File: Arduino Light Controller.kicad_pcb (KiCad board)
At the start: 2 copper layers, 120.5 x 39 mm, 44 parts, among them J1 Terminal - Pin - Male - 1x2 -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, J10 Terminal - Pin - Male - 1x2 -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, J11 Terminal - Pin - Male - 1x2 -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, J12 Terminal - Pin - Male - 1x2 -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, J13 Terminal - Pin - Male - 1x2 -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, J14 Terminal - Pin - Male - 1x2 -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, J15 Terminal - Pin - Male - 1x2 -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, J16 Terminal - Pin - Male - 1x2 -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, J17 Terminal - Pin - Male - 1x2 -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, J18 Terminal - Pin - Male - 1x2 -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, J19 Terminal - Pin - Male - 1x4 -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, J2 Terminal - Pin - Male - 1x2 -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, J20 Terminal - Pin - Male - 1x4 -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, J21 Terminal - Pin - Male - 1x4 -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, J22 Terminal - Pin - Male - 1x4 -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, J3 Terminal - Pin - Male - 1x2 -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, J4 Terminal - Pin - Male - 1x2 -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, J5 Terminal - Pin - Male - 1x2 -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, J6 Terminal - Pin - Male - 1x2 -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, J7 Terminal - Pin - Male - 1x2 -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, J8 Terminal - Pin - Male - 1x2 -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, J9 Terminal - Pin - Male - 1x2 -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

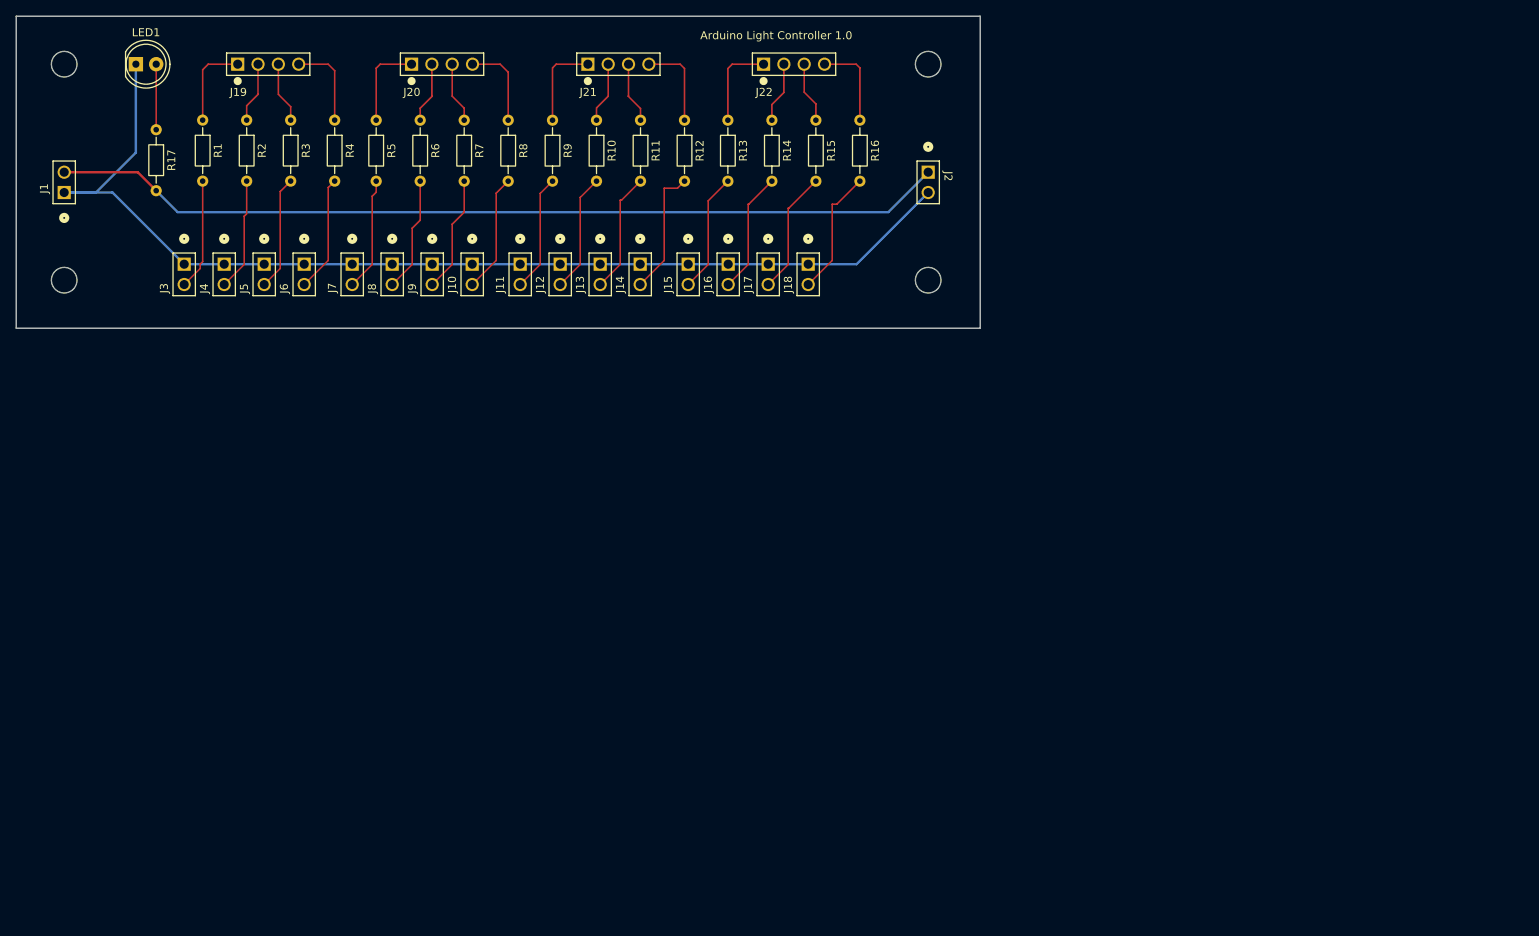
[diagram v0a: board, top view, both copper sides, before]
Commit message: New design to align with other boards and support power bus.
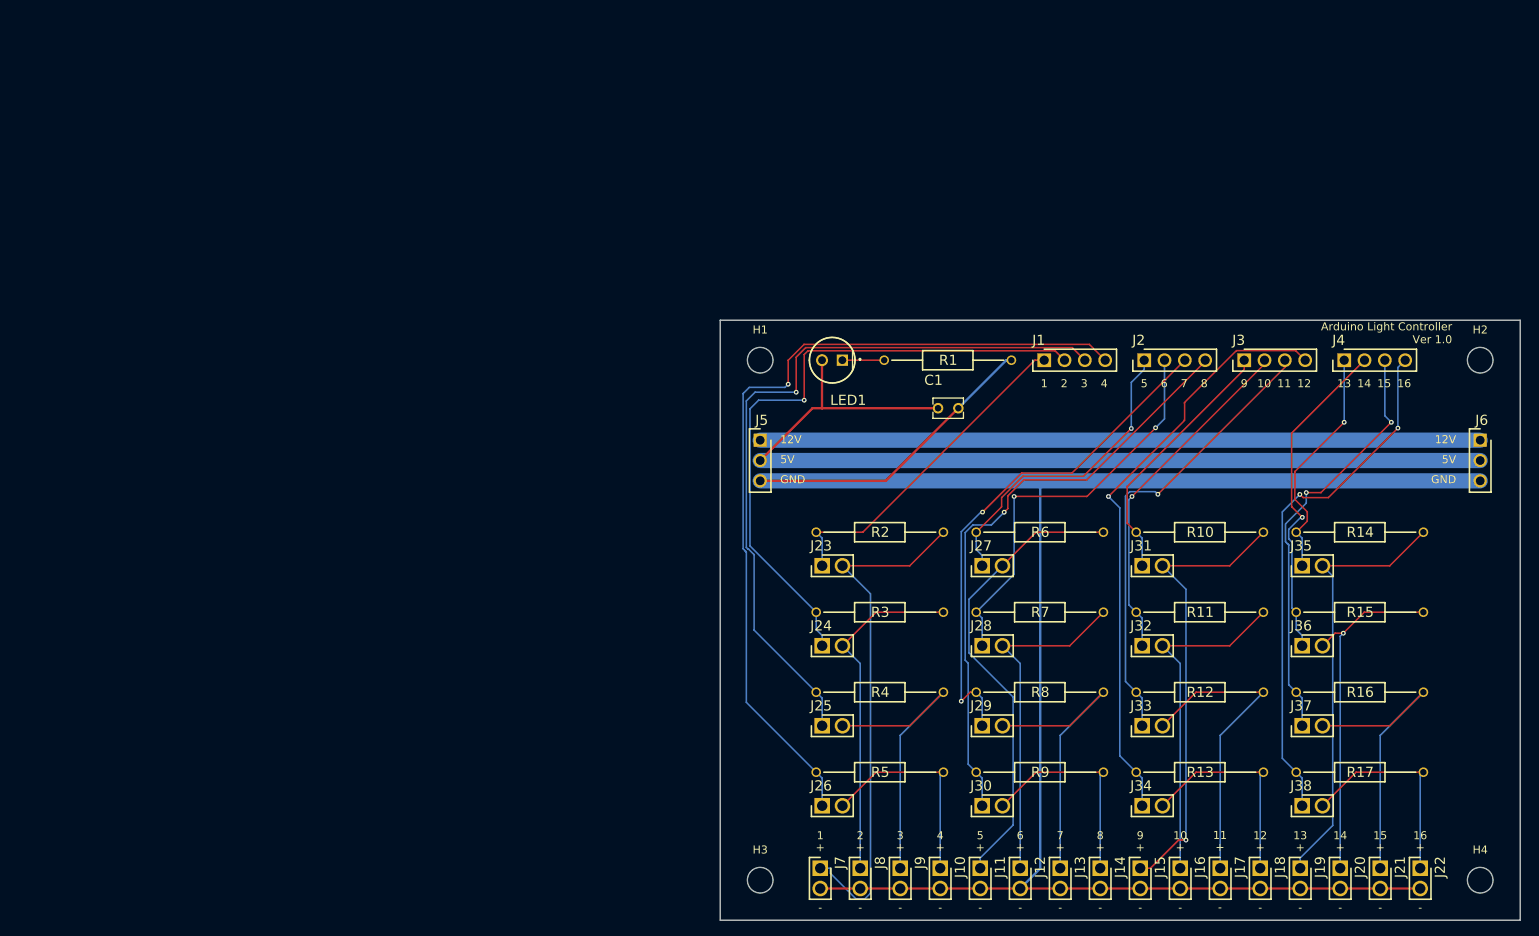
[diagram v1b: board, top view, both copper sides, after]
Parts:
- added C1: C315C104M5U5TA, SamacSys_Parts:C315C100J2G5TA, F.Cu at (128.5, 61.0)
- added J23: 61300211121, SamacSys_Parts:HDRV2W110P0X254_1X2_508X254X854P, F.Cu at (112.7, 80.7)
- added J24: 61300211121, SamacSys_Parts:HDRV2W110P0X254_1X2_508X254X854P, F.Cu at (112.7, 90.7)
- added J25: 61300211121, SamacSys_Parts:HDRV2W110P0X254_1X2_508X254X854P, F.Cu at (112.7, 100.7)
- added J26: 61300211121, SamacSys_Parts:HDRV2W110P0X254_1X2_508X254X854P, F.Cu at (112.7, 110.7)
- added J27: 61300211121, SamacSys_Parts:HDRV2W110P0X254_1X2_508X254X854P, F.Cu at (132.7, 80.7)
- added J28: 61300211121, SamacSys_Parts:HDRV2W110P0X254_1X2_508X254X854P, F.Cu at (132.7, 90.7)
- added J29: 61300211121, SamacSys_Parts:HDRV2W110P0X254_1X2_508X254X854P, F.Cu at (132.7, 100.7)
- added J30: 61300211121, SamacSys_Parts:HDRV2W110P0X254_1X2_508X254X854P, F.Cu at (132.7, 110.7)
- added J31: 61300211121, SamacSys_Parts:HDRV2W110P0X254_1X2_508X254X854P, F.Cu at (152.7, 80.7)
- added J32: 61300211121, SamacSys_Parts:HDRV2W110P0X254_1X2_508X254X854P, F.Cu at (152.7, 90.7)
- added J33: 61300211121, SamacSys_Parts:HDRV2W110P0X254_1X2_508X254X854P, F.Cu at (152.7, 100.7)
- added J34: 61300211121, SamacSys_Parts:HDRV2W110P0X254_1X2_508X254X854P, F.Cu at (152.7, 110.7)
- added J35: 61300211121, SamacSys_Parts:HDRV2W110P0X254_1X2_508X254X854P, F.Cu at (172.7, 80.7)
- added J36: 61300211121, SamacSys_Parts:HDRV2W110P0X254_1X2_508X254X854P, F.Cu at (172.7, 90.7)
- added J37: 61300211121, SamacSys_Parts:HDRV2W110P0X254_1X2_508X254X854P, F.Cu at (172.7, 100.7)
- added J38: 61300211121, SamacSys_Parts:HDRV2W110P0X254_1X2_508X254X854P, F.Cu at (172.7, 110.7)
- J1, J2, J3, J4: value Terminal - Pin - Male - 1x2 - 61300211121 -> 61300411121; footprint Digikey:Terminal - Pin - Male - 1x2 - 61300211121 -> SamacSys_Parts:HDRV4W95P0X254_1X4_1016X254X854P
- J10, J11, J12, J13, J14, J15, J16, J17, J18, J7, J8, J9: value Terminal - Pin - Male - 1x2 - 61300211121 -> 61300211121; footprint Digikey:Terminal - Pin - Male - 1x2 - 61300211121 -> SamacSys_Parts:HDRV2W110P0X254_1X2_508X254X854P
- J19, J20, J21, J22: value Terminal - Pin - Male - 1x4 - 61300411121 -> 61300211121; footprint Digikey:Terminal - Pin - Male - 1x4 - 61300411121 -> SamacSys_Parts:HDRV2W110P0X254_1X2_508X254X854P
- J5, J6: value Terminal - Pin - Male - 1x2 - 61300211121 -> 61300311121; footprint Digikey:Terminal - Pin - Male - 1x2 - 61300211121 -> SamacSys_Parts:HDRV3W64P0X254_1X3_762X254X869P
- LED1: value LED - Green - 5mm - LTL-307G -> WP7113GD; footprint Digikey:LED - Green - 5mm - LTL-307G -> SamacSys_Parts:L53ND
- R1, R10, R11, R12, R13, R14, R15, R16, R17, R2, R3, R4, R5, R6, R7, R8, R9: value 1K -> CFR-25JB-52-1K; footprint Resistor_THT:R_Axial_DIN0204_L3.6mm_D1.6mm_P7.62mm_Horizontal -> SamacSys_Parts:RESAD1590W60L630D240
- moved H4 192.2 mm to (195.0, 120.0)
- moved J19 166.5 mm to (172.5, 118.5), turned to -90 degrees
- moved R17 163.6 mm to (172.0, 106.5), turned to 0 degrees
- moved J20 153.5 mm to (177.5, 118.5), turned to -90 degrees
- moved J6 148.6 mm to (195.0, 65.0)
- moved J21 141.1 mm to (182.5, 118.5), turned to -90 degrees
- moved J4 140.5 mm to (178.0, 55.0), turned to 0 degrees
- moved J3 133.0 mm to (165.5, 55.0), turned to 0 degrees
- moved J22 129.8 mm to (187.5, 118.5), turned to -90 degrees
- moved J1 124.3 mm to (140.5, 55.0), turned to 0 degrees
- moved R5 98.3 mm to (112.0, 106.5), turned to 0 degrees
- moved R9 97.2 mm to (132.0, 106.5), turned to 0 degrees
- moved R13 96.2 mm to (152.0, 106.5), turned to 0 degrees
- moved LED1 95.7 mm to (115.3, 55.0), turned to 180 degrees
- moved J10 95.5 mm to (127.5, 118.5)
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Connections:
- J1 pad 1: GND -> /ResistorNet/In
- J1 pad 2: +5V -> /ResistorNet1/In
- J10 pad 1: GND -> /ResistorNet3/Out
- J10 pad 2: Net-(J10-Pad2) -> GND
- J11 pad 1: GND -> /ResistorNet4/Out
- J11 pad 2: Net-(J11-Pad2) -> GND
- J12 pad 1: GND -> /ResistorNet5/Out
- J12 pad 2: Net-(J12-Pad2) -> GND
- J13 pad 1: GND -> /ResistorNet6/Out
- J13 pad 2: Net-(J13-Pad2) -> GND
- J14 pad 1: GND -> /ResistorNet7/Out
- J14 pad 2: Net-(J14-Pad2) -> GND
- J15 pad 1: GND -> /ResistorNet8/Out
- J15 pad 2: Net-(J15-Pad2) -> GND
- J16 pad 1: GND -> /ResistorNet9/Out
- J16 pad 2: Net-(J16-Pad2) -> GND
- J17 pad 1: GND -> /ResistorNet10/Out
- J17 pad 2: Net-(J17-Pad2) -> GND
- J18 pad 1: GND -> /ResistorNet11/Out
- J18 pad 2: Net-(J18-Pad2) -> GND
- J19 pad 1: Net-(J19-Pad1) -> /ResistorNet12/Out
- J19 pad 2: Net-(J19-Pad2) -> GND
- J2 pad 1: +5V -> /ResistorNet4/In
- J2 pad 2: GND -> /ResistorNet5/In
- J20 pad 1: Net-(J20-Pad1) -> /ResistorNet13/Out
- J20 pad 2: Net-(J20-Pad2) -> GND
- J21 pad 1: Net-(J21-Pad1) -> /ResistorNet14/Out
- J21 pad 2: Net-(J21-Pad2) -> GND
- J22 pad 1: Net-(J22-Pad1) -> /ResistorNet15/Out
- J22 pad 2: Net-(J22-Pad2) -> GND
- J3 pad 1: GND -> /ResistorNet8/In
- J3 pad 2: Net-(J3-Pad2) -> /ResistorNet9/In
- J4 pad 1: GND -> /ResistorNet12/In
- J4 pad 2: Net-(J4-Pad2) -> /ResistorNet13/In
- J5 pad 1: GND -> +12V
- J5 pad 2: Net-(J5-Pad2) -> +5V
- J6 pad 1: GND -> +12V
- J6 pad 2: Net-(J6-Pad2) -> +5V
- J7 pad 1: GND -> /ResistorNet/Out
- J7 pad 2: Net-(J7-Pad2) -> GND
- J8 pad 1: GND -> /ResistorNet1/Out
- J8 pad 2: Net-(J8-Pad2) -> GND
- J9 pad 1: GND -> /ResistorNet2/Out
- J9 pad 2: Net-(J9-Pad2) -> GND
- LED1 pad 1: GND -> Net-(LED1-K)
- LED1 pad 2: Net-(LED1-A) -> +5V
- R1 pad 1: Net-(J19-Pad1) -> Net-(LED1-K)
- R1 pad 2: Net-(J3-Pad2) -> GND
- R10 pad 1: Net-(J21-Pad2) -> /ResistorNet8/In
- R10 pad 2: Net-(J12-Pad2) -> /ResistorNet8/Out
- R11 pad 1: Net-(J21-Pad3) -> /ResistorNet9/In
- R11 pad 2: Net-(J13-Pad2) -> /ResistorNet9/Out
- R12 pad 1: Net-(J21-Pad4) -> /ResistorNet10/In
- R12 pad 2: Net-(J14-Pad2) -> /ResistorNet10/Out
- R13 pad 1: Net-(J22-Pad1) -> /ResistorNet11/In
- R13 pad 2: Net-(J15-Pad2) -> /ResistorNet11/Out
- R14 pad 1: Net-(J22-Pad2) -> /ResistorNet12/In
- R14 pad 2: Net-(J16-Pad2) -> /ResistorNet12/Out
- R15 pad 1: Net-(J22-Pad3) -> /ResistorNet13/In
- R15 pad 2: Net-(J17-Pad2) -> /ResistorNet13/Out
- R16 pad 1: Net-(J22-Pad4) -> /ResistorNet14/In
- R16 pad 2: Net-(J18-Pad2) -> /ResistorNet14/Out
- R17 pad 1: Net-(LED1-A) -> /ResistorNet15/In
- R17 pad 2: +5V -> /ResistorNet15/Out
- R2 pad 1: Net-(J19-Pad2) -> /ResistorNet/In
- R2 pad 2: Net-(J4-Pad2) -> /ResistorNet/Out
- R3 pad 1: Net-(J19-Pad3) -> /ResistorNet1/In
- R3 pad 2: Net-(J5-Pad2) -> /ResistorNet1/Out
- R4 pad 1: Net-(J19-Pad4) -> /ResistorNet2/In
- R4 pad 2: Net-(J6-Pad2) -> /ResistorNet2/Out
- R5 pad 1: Net-(J20-Pad1) -> /ResistorNet3/In
- R5 pad 2: Net-(J7-Pad2) -> /ResistorNet3/Out
- R6 pad 1: Net-(J20-Pad2) -> /ResistorNet4/In
- R6 pad 2: Net-(J8-Pad2) -> /ResistorNet4/Out
- R7 pad 1: Net-(J20-Pad3) -> /ResistorNet5/In
- R7 pad 2: Net-(J9-Pad2) -> /ResistorNet5/Out
- R8 pad 1: Net-(J20-Pad4) -> /ResistorNet6/In
- R8 pad 2: Net-(J10-Pad2) -> /ResistorNet6/Out
- R9 pad 1: Net-(J21-Pad1) -> /ResistorNet7/In
- R9 pad 2: Net-(J11-Pad2) -> /ResistorNet7/Out
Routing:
- net GND: track 137.5 -> 254.6 mm
- net /ResistorNet3/In: track 0.00 -> 106.2 mm, vias 0 -> 1
- net /ResistorNet2/In: track 0.00 -> 92.9 mm, vias 0 -> 1
- net +12V: track 0.00 -> 90.0 mm
- net /ResistorNet1/In: track 0.00 -> 79.5 mm, vias 0 -> 1
- net /ResistorNet7/In: track 0.00 -> 75.0 mm, vias 0 -> 1
- net /ResistorNet11/In: track 0.00 -> 74.4 mm, vias 0 -> 1
- net /ResistorNet15/In: track 0.00 -> 65.7 mm, vias 0 -> 2
- net /ResistorNet6/In: track 0.00 -> 65.7 mm, vias 0 -> 2
- net /ResistorNet/Out: track 0.00 -> 65.3 mm
- net /ResistorNet4/Out: track 0.00 -> 57.9 mm
- net /ResistorNet10/In: track 0.00 -> 57.3 mm, vias 0 -> 1
- net /ResistorNet8/Out: track 0.00 -> 57.0 mm, vias 0 -> 1
- net /ResistorNet12/Out: track 0.00 -> 54.4 mm
- net /ResistorNet14/In: track 0.00 -> 53.7 mm, vias 0 -> 2
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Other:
- board size 120.5 x 39 mm -> 100 x 75 mm
- board text added: "+"
- board text added: "-"
- board text added: "1"
- board text added: "10"
- board text added: "11"
- board text added: "12"
- board text added: "12V"
- board text added: "13"
- board text added: "14"
- board text added: "15"
- board text added: "16"
- board text added: "2"
- board text added: "3"
- board text added: "4"
- board text added: "5"
- board text added: "5V"
- board text added: "6"
- board text added: "7"
- board text added: "8"
- board text added: "9"
- board text added: "Arduino Light Controller Ver 1.0"
- board text added: "GND"
- board text removed: "Arduino Light Controller 1.0"

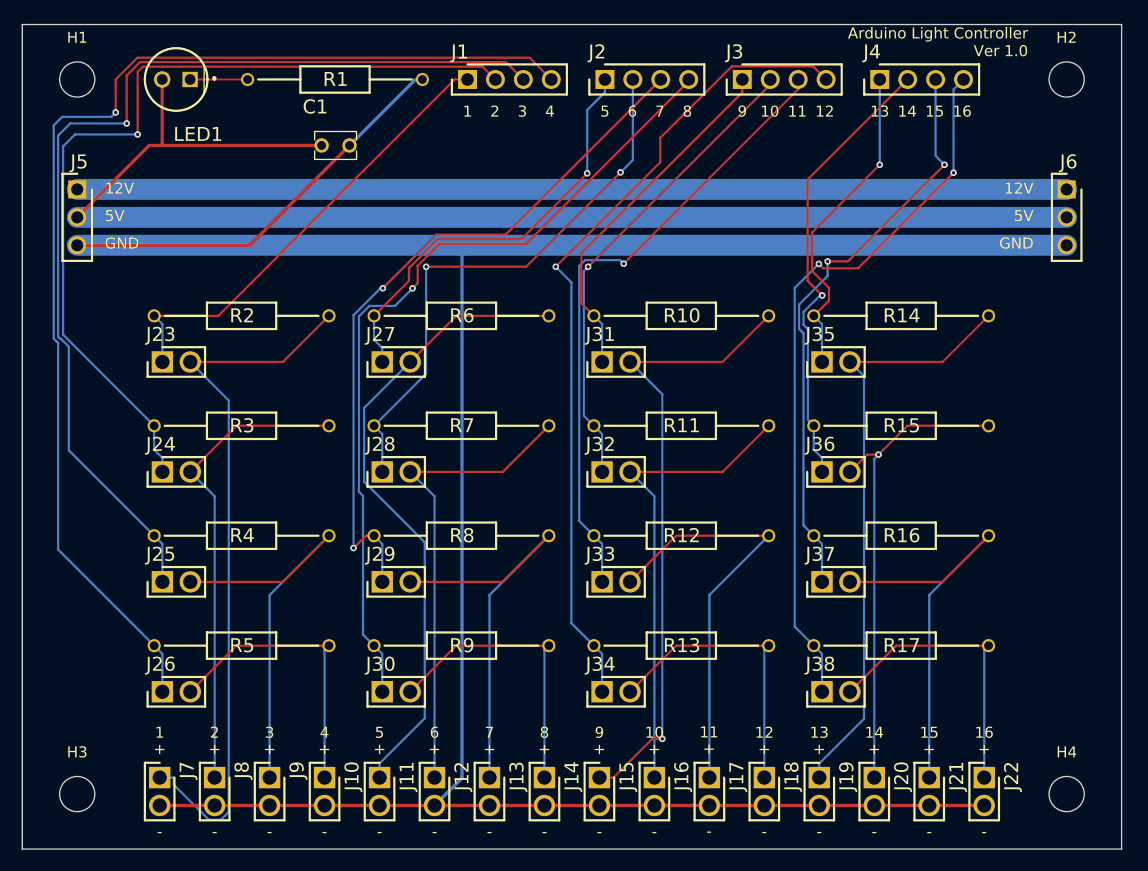
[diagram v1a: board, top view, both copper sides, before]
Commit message: Updated re-annotated the schematics, created new PCB based on standards and updated components.
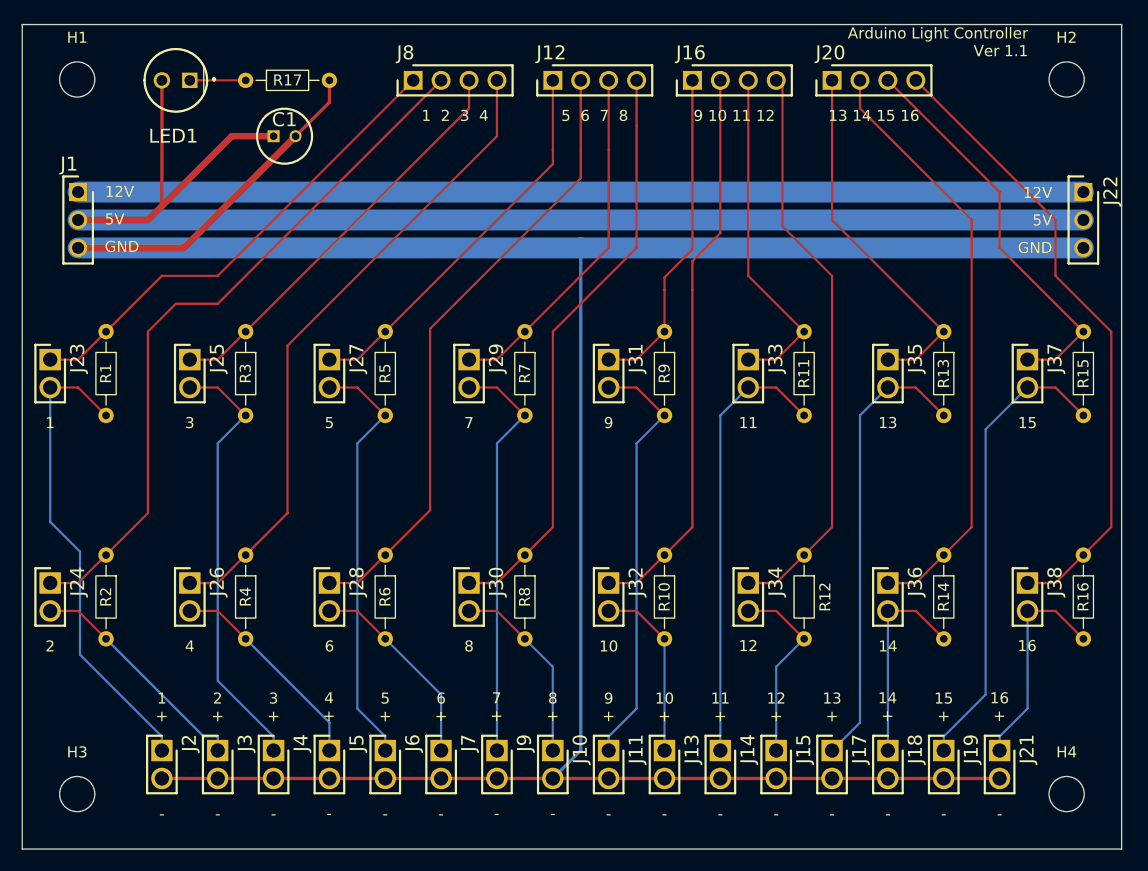
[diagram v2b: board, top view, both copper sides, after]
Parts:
- C1: value C315C104M5U5TA -> 860010472002; footprint SamacSys_Parts:C315C100J2G5TA -> SamacSys_Parts:CAPPRD200W52D500H1250
- J1: value 61300411121 -> 61300311121; footprint SamacSys_Parts:HDRV4W95P0X254_1X4_1016X254X854P -> SamacSys_Parts:HDRV3W64P0X254_1X3_762X254X869P
- J12, J16, J20, J8: value 61300211121 -> 61300411121; footprint SamacSys_Parts:HDRV2W110P0X254_1X2_508X254X854P -> SamacSys_Parts:HDRV4W95P0X254_1X4_1016X254X854P
- J2, J3, J4: value 61300411121 -> 61300211121; footprint SamacSys_Parts:HDRV4W95P0X254_1X4_1016X254X854P -> SamacSys_Parts:HDRV2W110P0X254_1X2_508X254X854P
- J22: value 61300211121 -> 61300311121; footprint SamacSys_Parts:HDRV2W110P0X254_1X2_508X254X854P -> SamacSys_Parts:HDRV3W64P0X254_1X3_762X254X869P
- J5, J6: value 61300311121 -> 61300211121; footprint SamacSys_Parts:HDRV3W64P0X254_1X3_762X254X869P -> SamacSys_Parts:HDRV2W110P0X254_1X2_508X254X854P
- R1, R10, R11, R12, R13, R14, R15, R16, R17, R2, R3, R4, R5, R6, R7, R8, R9: footprint SamacSys_Parts:RESAD1590W60L630D240 -> Resistor_THT:R_Axial_DIN0204_L3.6mm_D1.6mm_P7.62mm_Horizontal
- moved J4 82.3 mm to (122.9, 116.0), turned to -90 degrees
- moved J6 80.3 mm to (133.0, 116.0)
- moved J3 77.5 mm to (117.8, 116.0), turned to -90 degrees
- moved J2 73.1 mm to (112.7, 116.0), turned to -90 degrees
- moved R17 72.9 mm to (120.3, 55.1)
- moved J8 65.9 mm to (135.6, 55.1), turned to 0 degrees
- moved J12 64.3 mm to (148.3, 55.1), turned to 0 degrees
- moved J20 63.5 mm to (173.7, 55.1), turned to 0 degrees
- moved J16 63.5 mm to (161.0, 55.1), turned to 0 degrees
- moved J5 56.0 mm to (127.9, 116.0)
- moved J22 54.0 mm to (196.5, 65.2)
- moved R13 42.8 mm to (183.8, 77.9), turned to -90 degrees
- moved R9 38.9 mm to (158.4, 77.9), turned to -90 degrees
- moved J1 36.9 mm to (105.1, 65.2), turned to -90 degrees
- moved R5 35.5 mm to (133.0, 77.9), turned to -90 degrees
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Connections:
- J1 pad 1: /ResistorNet/In -> +12V
- J1 pad 2: /ResistorNet1/In -> +5V
- J1 pad 3: /ResistorNet2/In -> GND
- J10 pad 1: /ResistorNet3/Out -> /ResistorNet7/Out
- J11 pad 1: /ResistorNet4/Out -> /ResistorNet8/Out
- J12 pad 1: /ResistorNet5/Out -> /ResistorNet4/In
- J12 pad 2: GND -> /ResistorNet5/In
- J13 pad 1: /ResistorNet6/Out -> /ResistorNet9/Out
- J14 pad 1: /ResistorNet7/Out -> /ResistorNet10/Out
- J15 pad 1: /ResistorNet8/Out -> /ResistorNet11/Out
- J16 pad 1: /ResistorNet9/Out -> /ResistorNet8/In
- J16 pad 2: GND -> /ResistorNet9/In
- J17 pad 1: /ResistorNet10/Out -> /ResistorNet12/Out
- J18 pad 1: /ResistorNet11/Out -> /ResistorNet13/Out
- J19 pad 1: /ResistorNet12/Out -> /ResistorNet14/Out
- J2 pad 1: /ResistorNet4/In -> /ResistorNet/Out
- J2 pad 2: /ResistorNet5/In -> GND
- J20 pad 1: /ResistorNet13/Out -> /ResistorNet12/In
- J20 pad 2: GND -> /ResistorNet13/In
- J21 pad 1: /ResistorNet14/Out -> /ResistorNet15/Out
- J22 pad 1: /ResistorNet15/Out -> +12V
- J22 pad 2: GND -> +5V
- J3 pad 1: /ResistorNet8/In -> /ResistorNet1/Out
- J3 pad 2: /ResistorNet9/In -> GND
- J4 pad 1: /ResistorNet12/In -> /ResistorNet2/Out
- J4 pad 2: /ResistorNet13/In -> GND
- J5 pad 1: +12V -> /ResistorNet3/Out
- J5 pad 2: +5V -> GND
- J6 pad 1: +12V -> /ResistorNet4/Out
- J6 pad 2: +5V -> GND
- J7 pad 1: /ResistorNet/Out -> /ResistorNet5/Out
- J8 pad 1: /ResistorNet1/Out -> /ResistorNet/In
- J8 pad 2: GND -> /ResistorNet1/In
- J9 pad 1: /ResistorNet2/Out -> /ResistorNet6/Out
- R1 pad 1: Net-(LED1-K) -> /ResistorNet/In
- R1 pad 2: GND -> /ResistorNet/Out
- R10 pad 1: /ResistorNet8/In -> /ResistorNet9/In
- R10 pad 2: /ResistorNet8/Out -> /ResistorNet9/Out
- R11 pad 1: /ResistorNet9/In -> /ResistorNet10/In
- R11 pad 2: /ResistorNet9/Out -> /ResistorNet10/Out
- R12 pad 1: /ResistorNet10/In -> /ResistorNet11/In
- R12 pad 2: /ResistorNet10/Out -> /ResistorNet11/Out
- R13 pad 1: /ResistorNet11/In -> /ResistorNet12/In
- R13 pad 2: /ResistorNet11/Out -> /ResistorNet12/Out
- R14 pad 1: /ResistorNet12/In -> /ResistorNet13/In
- R14 pad 2: /ResistorNet12/Out -> /ResistorNet13/Out
- R15 pad 1: /ResistorNet13/In -> /ResistorNet14/In
- R15 pad 2: /ResistorNet13/Out -> /ResistorNet14/Out
- R16 pad 1: /ResistorNet14/In -> /ResistorNet15/In
- R16 pad 2: /ResistorNet14/Out -> /ResistorNet15/Out
- R17 pad 1: /ResistorNet15/In -> Net-(LED1-K)
- R17 pad 2: /ResistorNet15/Out -> GND
- R2 pad 1: /ResistorNet/In -> /ResistorNet1/In
- R2 pad 2: /ResistorNet/Out -> /ResistorNet1/Out
- R3 pad 1: /ResistorNet1/In -> /ResistorNet2/In
- R3 pad 2: /ResistorNet1/Out -> /ResistorNet2/Out
- R4 pad 1: /ResistorNet2/In -> /ResistorNet3/In
- R4 pad 2: /ResistorNet2/Out -> /ResistorNet3/Out
- R5 pad 1: /ResistorNet3/In -> /ResistorNet4/In
- R5 pad 2: /ResistorNet3/Out -> /ResistorNet4/Out
- R6 pad 1: /ResistorNet4/In -> /ResistorNet5/In
- R6 pad 2: /ResistorNet4/Out -> /ResistorNet5/Out
- R7 pad 1: /ResistorNet5/In -> /ResistorNet6/In
- R7 pad 2: /ResistorNet5/Out -> /ResistorNet6/Out
- R8 pad 1: /ResistorNet6/In -> /ResistorNet7/In
- R8 pad 2: /ResistorNet6/Out -> /ResistorNet7/Out
- R9 pad 1: /ResistorNet7/In -> /ResistorNet8/In
- R9 pad 2: /ResistorNet7/Out -> /ResistorNet8/Out
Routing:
- net /ResistorNet2/In: track 92.9 -> 37.4 mm, vias 1 -> 0
- net /ResistorNet3/In: track 106.2 -> 58.8 mm, vias 1 -> 0
- net /ResistorNet6/In: track 65.7 -> 32.1 mm, vias 2 -> 0
- net /ResistorNet9/Out: track 43.1 -> 16.3 mm
- net /ResistorNet10/In: track 57.3 -> 31.1 mm, vias 1 -> 0
- net /ResistorNet13/Out: track 43.9 -> 18.8 mm, vias 1 -> 0
- net /ResistorNet5/Out: track 43.1 -> 18.4 mm
- net /ResistorNet/Out: track 65.3 -> 43.4 mm
- net /ResistorNet11/In: track 74.4 -> 52.5 mm, vias 1 -> 0
- net /ResistorNet1/Out: track 43.1 -> 21.2 mm
- net /ResistorNet7/In: track 75.0 -> 53.5 mm, vias 1 -> 0
- net /ResistorNet4/Out: track 57.9 -> 38.7 mm
- net /ResistorNet8/Out: track 57.0 -> 38.7 mm, vias 1 -> 0
- net /ResistorNet14/In: track 53.7 -> 36.4 mm, vias 2 -> 0
- net /ResistorNet1/In: track 79.5 -> 64.2 mm, vias 1 -> 0
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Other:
- board text added: "1 +"
- board text added: "1 2 3 4"
- board text added: "10 +"
- board text added: "11 +"
- board text added: "12 +"
- board text added: "13 +"
- board text added: "13 14 15 16"
- board text added: "14 +"
- board text added: "15 +"
- board text added: "16 +"
- board text added: "2 +"
- board text added: "3 +"
- board text added: "4 +"
- board text added: "5 +"
- board text added: "5 6 7 8"
- board text added: "6 +"
- board text added: "7 +"
- board text added: "8 +"
- board text added: "9 +"
- board text added: "9 10 11 12"
- board text added: "Arduino Light Controller Ver 1.1"
- board text removed: "+"
- board text removed: "Arduino Light Controller Ver 1.0"
